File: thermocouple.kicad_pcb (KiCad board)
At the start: 2 copper layers, 39 parts, among them CON1 AVR-ISP-6, IC1 SP3485CN, IC2 ATTINY1634-S, P1 CONN_2, P2 CONN_4, U1 AD8237, U2 TC1047, U3 7805, U4 LM358, X1 CRYSTAL

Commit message: visko daug
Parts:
- added 1PIN_SMD: P***, 1PIN_SMD, F.Cu at (250.4, 150.1)
- added 1PIN_SMD: P***, 1PIN_SMD, F.Cu at (229.5, 150.4)
- added ?: , hole3mm, F.Cu at (215.4, 149.9)
- added C17: 100nF, SM0603_Capa, F.Cu at (265.0, 151.3)
- C1, C12, C5, CON1, JP1, P2, X1: moved to B.Cu
- IC2: value ATTINY1634-S -> ATMEGA88-A; footprint SO20L -> TQFP32
- R9: value 120 -> 10k
- U3: footprint TO220 -> LM78XXV; moved to B.Cu
- moved CON1 270.5 mm to (205.4, 176.0), turned to 270 degrees
- moved C2 93.3 mm to (255.0, 141.9), turned to 180 degrees
- moved L1 90.6 mm to (254.9, 140.1), turned to 180 degrees
- moved C4 90.4 mm to (254.9, 138.2), turned to 0 degrees
- moved D???1 84.4 mm to (251.7, 141.4), turned to 270 degrees
- moved R5 84.1 mm to (251.7, 138.8), turned to 90 degrees
- moved P1 82.4 mm to (240.0, 150.0), turned to 270 degrees
- moved P2 73.3 mm to (261.2, 150.0), turned to 90 degrees
- moved C15 72.4 mm to (257.3, 163.6)
- moved U2 72.2 mm to (235.3, 137.5)
- moved R1 72.0 mm to (241.8, 141.1), turned to 0 degrees
- moved C14 69.6 mm to (241.3, 161.9), turned to 90 degrees
- moved C7 66.0 mm to (243.1, 134.5), turned to 0 degrees
- moved X1 65.8 mm to (239.5, 162.3), turned to 135 degrees
- moved C6 65.5 mm to (254.1, 131.2), turned to 225 degrees
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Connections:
- net N-0000010 renamed /VTHERMO_FILTERED
- net N-0000013 renamed /TERMINATOR
- net N-000002 renamed /FB
- net N-000004 renamed /THERMOCOUPLE+
- C14 pad 1: N-0000018 -> N-0000016
- IC1 pad 1: N-0000026 -> /RX
- IC1 pad 2: N-0000029 -> //RE
- IC1 pad 3: N-0000029 -> //RE
- IC1 pad 4: N-0000031 (its old number) -> /TX
- IC1 pad 7: /B -> VDD
- IC2 pad 1: N-0000031 (its old number) -> N-0000041
- IC2 pad 10: GND -> N-0000037
- IC2 pad 11: VDD -> N-0000036
- IC2 pad 12: N-0000018 -> N-0000028
- IC2 pad 13: N-000007 -> N-0000026
- IC2 pad 14: N-000005 -> N-0000025
- IC2 pad 18: N-0000033 (its old number) -> VAA
- IC2 pad 2: N-0000026 -> N-0000040
- IC2 pad 20: N-0000019 -> /AREF
- IC2 pad 3: N-0000029 -> GND
- IC2 pad 4: N-0000023 (its old number) -> VDD
- IC2 pad 5: /THERMOCOUPLE -> GND
- IC2 pad 6: /AMBIENT_TEMP -> VDD
- IC2 pad 7: N-0000017 (its old number) -> N-0000016
- IC2 pad 8: N-0000021 (its old number) -> N-000007
- IC2 pad 9: /AREF -> N-0000038
- P1 pad 1: N-000003 (its old number) -> /THERMOCOUPLE-
- R1 pad 1: N-000003 (its old number) -> /THERMOCOUPLE-
- R9 pad 1: N-000005 -> VDD
- R9 pad 2: VDD -> N-0000014
- U1 pad 3: N-000003 (its old number) -> /THERMOCOUPLE-
- U4 pad 6: /THERMOCOUPLE -> /VTHERMO_BUFFERED
- U4 pad 7: /THERMOCOUPLE -> /VTHERMO_BUFFERED
- X1 pad 1: N-0000018 -> N-0000016
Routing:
- net /VTHERMO_BUFFERED: track 0.00 -> 64.4 mm
- net /AMBIENT_TEMP: track 2.09 -> 60.4 mm
- net VAA: track 33.8 -> 47.9 mm, vias 0 -> 1
- net N-0000046: track 15.4 -> 2.33 mm
- net N-000003 (its old number): track 12.2 -> 0.00 mm
- net /THERMOCOUPLE+: track 12.2 -> 0.00 mm
- net VCC: track 1.64 -> 11.0 mm
- net GND: track 6.69 -> 1.41 mm
- net N-0000016: track 0.00 -> 5.21 mm
- net VDD: track 2.43 -> 7.53 mm
- net /AREF: track 6.62 -> 1.54 mm
- net /VTHERMO_FILTERED: track 15.6 -> 10.6 mm
- net N-000007: track 0.00 -> 3.65 mm
- net /THERMOCOUPLE: track 0.65 -> 0.00 mm
- added copper zone on B.Cu, net GND
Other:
- board outline added: 54.9 x 54.9 mm

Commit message: blah
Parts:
- removed P1: CONN_2, PIN_ARRAY_2X1
- added ?: , hole3mm, F.Cu at (238.3, 172.6)
- added ?: , hole3mm, F.Cu at (256.4, 148.7)
- added C18: 100nF, SM0603_Capa, F.Cu at (229.4, 137.0)
- added C19: 10uF, SM0805, B.Cu at (237.2, 134.2)
- added C20: 100nF, SM0603_Capa, B.Cu at (232.7, 127.3)
- added C21: 100nF, SM0603_Capa, F.Cu at (273.9, 144.0)
- added C22: 10nF, SM0603_Capa, F.Cu at (269.4, 140.3)
- added C23: 1nF, SM0603_Capa, F.Cu at (269.4, 138.4)
- added D1: DIODE, DO-214AA(SMB), F.Cu at (262.4, 141.2)
- added D2: DIODE, DO-214AC(SMA), F.Cu at (224.9, 183.6)
- added D3: DIODE, DO-214AC(SMA), F.Cu at (223.9, 190.1)
- added R11: 1k, SM0603_Resistor, F.Cu at (243.1, 134.0)
- added R12: 1k 1%, SM0603_Resistor, F.Cu at (234.9, 126.6)
- added R13: 100k 1%, SM0603_Resistor, F.Cu at (232.7, 127.3)
- added R14: 10k, SM0603_Resistor, F.Cu at (230.0, 133.7)
- added R15: 1k, SM0603_Resistor, F.Cu at (252.5, 138.8)
- 1PIN_SMD (x2), C16, C17, C7: moved to B.Cu
- R2: value R -> 1k 0.1%; footprint SM0603 -> SM0805
- R3: value R -> 100k 0.1%; footprint SM0603 -> SM0805
- R4, R6: value 1k -> 1k 0.1%; footprint SM0603 -> SM0805
- R5: value R -> 1k
- U4: value LM358 -> MCP6L01
- moved C16 47.9 mm to (251.1, 156.1), turned to 0 degrees
- moved CON1 42.8 mm to (247.5, 168.8)
- moved C17 39.7 mm to (227.3, 163.8), turned to 270 degrees
- moved R9 37.5 mm to (241.9, 166.4), turned to 270 degrees
- moved IC1 17.0 mm to (255.9, 161.5), turned to 0 degrees
- moved JP1 13.1 mm to (259.7, 160.9), turned to 90 degrees
- moved C3 12.3 mm to (270.0, 135.2)
- moved R8 9.38 mm to (261.6, 161.7), turned to 270 degrees
- moved 1PIN_SMD 8.89 mm to (231.6, 141.7), turned to 90 degrees
- moved 1PIN_SMD 8.72 mm to (248.0, 141.7), turned to 270 degrees
- moved C15 7.10 mm to (256.0, 156.6), turned to 0 degrees
- moved C1 3.84 mm to (257.2, 141.1), turned to 45 degrees
- moved C5 3.02 mm to (251.5, 129.5), turned to 335 degrees
- moved R1 2.96 mm to (244.0, 139.1), turned to 90 degrees
- moved C2 2.60 mm to (257.6, 141.9)
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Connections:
- 1PIN_SMD pad 1: (no net) -> /THERMOCOUPLE-
- 1PIN_SMD pad 1: (no net) -> /THERMOCOUPLE+
- CON1 pad 1: N-0000011 (its old number) -> /MISO
- CON1 pad 2: N-0000035 -> VDD
- CON1 pad 3: N-0000034 -> /SCK
- CON1 pad 4: N-0000033 -> /MOSI
- CON1 pad 5: N-0000032 -> /RESET
- CON1 pad 6: N-0000031 -> GND
- IC1 pad 7: VDD -> /B
- IC1 pad 8: (no net) -> VDD
- IC2 pad 15: N-0000024 -> /MOSI
- IC2 pad 16: N-0000023 -> /MISO
- IC2 pad 17: N-0000021 -> /SCK
- IC2 pad 24: /VTHERMO_BUFFERED -> /VTHERMO_FILTERED
- IC2 pad 29: N-0000014 (its old number) -> /RESET
- P2 pad 2: /B -> /A
- P2 pad 3: /A -> /B
- P2 pad 4: VCC -> N-0000038
- R1 pad 2: GND -> N-0000045
- R2 pad 1: GND -> /FB
- R2 pad 2: /FB -> N-0000045
- R6 pad 2: /AMBIENT_TEMP -> N-0000048
- R9 pad 2: N-0000014 (its old number) -> /RESET
- U1 pad 6: GND -> N-0000030
- U4 pad 1: /AMBIENT_TEMP -> N-0000048
- U4 pad 5: /VTHERMO_FILTERED -> N-0000028
- U4 pad 6: /VTHERMO_BUFFERED -> N-0000045
- U4 pad 7: /VTHERMO_BUFFERED -> N-0000045
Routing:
- net /AREF: track 1.54 -> 94.1 mm, vias 0 -> 5
- net VDD: track 7.53 -> 74.7 mm, vias 0 -> 2
- net /VTHERMO_BUFFERED: track 64.4 -> 0.00 mm
- net VAA: track 47.9 -> 105.5 mm, vias 1 -> 6
- net /VTHERMO_FILTERED: track 10.6 -> 61.0 mm
- net GND: track 1.41 -> 49.7 mm, vias 0 -> 24
- net /TX: track 0.00 -> 33.8 mm
- net /RX: track 0.00 -> 32.2 mm
- net //RE: track 0.00 -> 30.7 mm
- net /B: track 0.00 -> 28.2 mm
- net /SCK: track 0.00 -> 26.8 mm, vias 0 -> 1
- net /MISO: track 0.00 -> 24.0 mm, vias 0 -> 1
- net /MOSI: track 0.00 -> 22.9 mm, vias 0 -> 2
- net N-0000045: track 0.00 -> 22.1 mm, vias 0 -> 2
- net /RESET: track 0.00 -> 22.1 mm, vias 0 -> 2
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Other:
- board size 54.9 x 54.9 mm -> 55 x 55 mm
- net class Default: via_dia 0.889 -> 0.762; via_drill 0.635 -> 0.381
- net class power: via_dia 0.889 -> 0.762; via_drill 0.635 -> 0.381
- rule via_min_drill: 0.508 -> 0.381
- rule via_min_size: 0.889 -> 0.762

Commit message: suddenly everything went better than expected
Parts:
- added D4: LED, SM0805, B.Cu at (227.6, 159.2)
- added D5: LED, SM0805, B.Cu at (227.6, 161.4)
- added R10: 1k, SM0603_Resistor, B.Cu at (224.3, 159.2)
- added R16: 1k, SM0603_Resistor, B.Cu at (224.3, 161.4)
- C1, C5: footprint c_tant_E -> C1V8
- C3: moved to B.Cu
- CON1: moved to F.Cu
- R1, R5, R7, R8, R9: footprint SM0603 -> SM0603_Resistor
- moved C5 25.6 mm to (253.7, 155.0), turned to 90 degrees
- moved CON1 24.8 mm to (227.4, 154.2)
- moved C3 11.8 mm to (258.4, 137.6), turned to 225 degrees
- moved C23 9.63 mm to (274.0, 146.9)
- moved C6 6.74 mm to (249.0, 135.6), turned to 180 degrees
- moved L2 6.28 mm to (248.9, 133.6), turned to 180 degrees
- moved R8 5.84 mm to (260.6, 156.0), turned to 180 degrees
- moved C8 4.78 mm to (247.2, 131.4), turned to 180 degrees
- moved C1 4.47 mm to (255.1, 145.0), turned to 180 degrees
- moved C9 3.05 mm to (247.2, 129.5), turned to 180 degrees
- moved IC1 2.79 mm to (253.4, 160.3), turned to 270 degrees
- moved C10 2.39 mm to (247.2, 127.7), turned to 180 degrees
- moved JP1 2.26 mm to (261.3, 159.3), turned to 270 degrees
- moved C17 2.19 mm to (225.1, 163.9)
- moved C22 1.47 mm to (269.6, 138.9)
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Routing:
- net GND: track 49.7 -> 123.1 mm, vias 24 -> 66
- net VDD: track 74.7 -> 97.5 mm, vias 2 -> 5
- net /SCK: track 26.8 -> 9.85 mm, vias 1 -> 0
- net /MOSI: track 22.9 -> 7.30 mm, vias 2 -> 0
- net /B: track 28.2 -> 14.4 mm
- net /MISO: track 24.0 -> 11.2 mm, vias 1 -> 0
- net /A: track 17.4 -> 29.8 mm
- net /TX: track 33.8 -> 21.8 mm
- net //RE: track 30.7 -> 20.8 mm
- net /RX: track 32.2 -> 24.2 mm
- net /AREF: track 94.1 -> 87.1 mm
- net N-0000027: track 0.00 -> 6.24 mm, vias 0 -> 1
- net N-0000026: track 0.00 -> 5.84 mm, vias 0 -> 1
- net VCC: track 10.5 -> 16.0 mm
- net /RESET: track 22.1 -> 27.6 mm
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
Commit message: almost there
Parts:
- removed D2, D3: DIODE, DO-214AC(SMA)
- removed P2: CONN_4, PIN_ARRAY_4x1
- added C101: 100nF, SM0603_Capa, F.Cu at (222.8, 132.2)
- added C102: 100nF, SM0603_Capa, B.Cu at (236.9, 165.3)
- added C103: 100nF, SM0603_Capa, B.Cu at (234.0, 163.2)
- added C104: 100nF, SM0603_Capa, F.Cu at (225.1, 145.9)
- added C105: 100nF, SM0603_Capa, B.Cu at (227.7, 165.0)
- added C106: 100nF, SM0603_Capa, B.Cu at (246.0, 165.4)
- added C107: 10uF, SM0805, F.Cu at (220.9, 165.3)
- added P10: 12AC, conn35, B.Cu at (262.3, 146.1)
- added P10: 12AC, conn35, B.Cu at (262.3, 153.7)
- added R17: 1k, SM0603_Resistor, F.Cu at (233.8, 140.9)
- added R18: 1k, SM0603_Resistor, F.Cu at (244.1, 139.7)
- C21: moved to B.Cu
- moved C21 43.9 mm to (234.2, 125.5)
- moved C23 23.4 mm to (253.1, 136.4)
- moved C22 13.9 mm to (255.9, 136.4), turned to 180 degrees
- moved R8 3.29 mm to (259.0, 158.9), turned to 90 degrees
- moved C16 3.27 mm to (247.9, 155.3), turned to 90 degrees
- moved D1 2.21 mm to (261.6, 139.7)
- moved R1 1.78 mm to (244.0, 137.3)
- moved C19 1.73 mm to (238.4, 132.9)
- moved C1 0.99 mm to (254.6, 144.1)
- moved C5 0.76 mm to (253.0, 154.9)
- moved JP1 0.74 mm to (261.1, 160.0)
- moved C12 0.27 mm to (232.1, 130.7)
- moved C2 0.23 mm to (257.4, 142.0)
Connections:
- C21 pad 1: N-0000025 -> N-000007
- C22 pad 1: N-0000024 -> N-0000049
- C23 pad 1: N-0000023 -> N-0000049
- C4 pad 1: N-0000052 -> N-0000049
- D1 pad 1: N-0000035 -> /VIN
- L1 pad 2: N-0000052 -> N-0000049
- R12 pad 2: N-0000036 -> N-000007
- R13 pad 1: N-0000036 -> N-000007
- R15 pad 2: N-0000052 -> N-0000049
- R5 pad 2: N-0000052 -> N-0000049
- U1 pad 2: /THERMOCOUPLE+ -> N-0000030
- U1 pad 3: /THERMOCOUPLE- -> N-0000029
- U4 pad 5: N-0000036 -> N-000007
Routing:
- net GND: track 123.1 -> 161.0 mm, vias 66 -> 84
- net N-0000049: track 0.00 -> 9.76 mm
- net /A: track 29.8 -> 21.3 mm
- net /THERMOCOUPLE+: track 9.55 -> 1.88 mm
- net N-000007: track 0.00 -> 7.40 mm, vias 0 -> 1
- net N-0000030: track 0.00 -> 6.47 mm
- net N-0000052: track 6.23 -> 0.00 mm
- net N-0000029: track 0.00 -> 4.21 mm
- net N-0000036: track 4.11 -> 0.00 mm
- net /AREF: track 87.1 -> 91.0 mm, vias 5 -> 6
- net VAA: track 107.4 -> 111.1 mm
- net /THERMOCOUPLE-: track 9.48 -> 6.04 mm
- net /VIN: track 0.00 -> 2.86 mm
- net /B: track 14.4 -> 11.8 mm
- net N-0000035: track 2.33 -> 0.00 mm
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
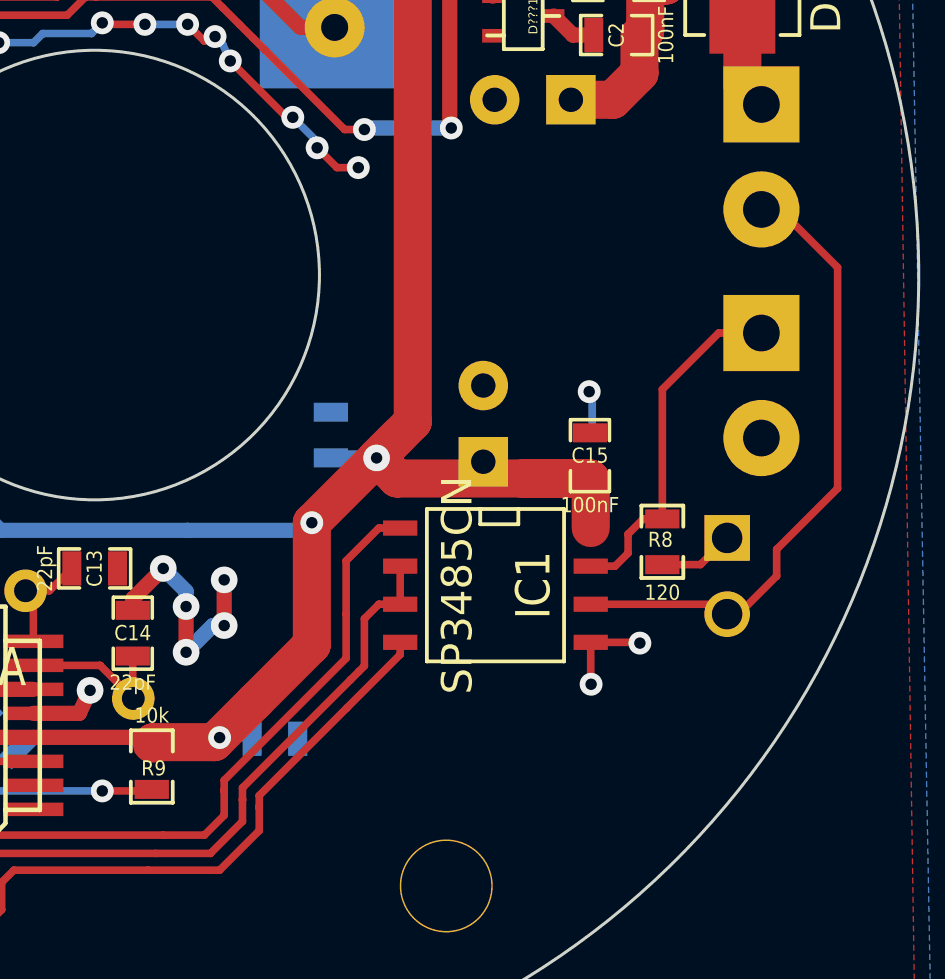
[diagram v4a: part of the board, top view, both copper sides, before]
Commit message: RS485 protection added
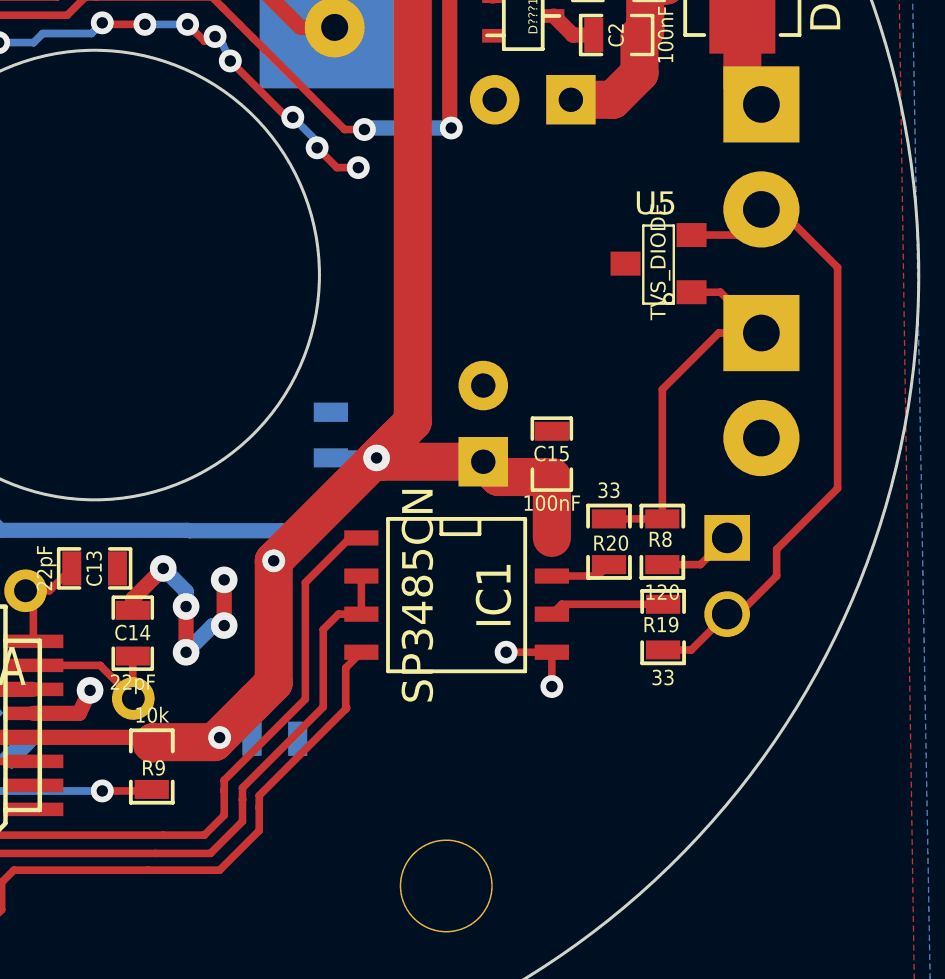
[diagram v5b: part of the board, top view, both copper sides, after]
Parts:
- added R19: 33, SM0603_Resistor, F.Cu at (259.0, 161.7)
- added R20: 33, SM0603_Resistor, F.Cu at (257.2, 158.9)
- added U5: TVS_DIODE, SOT23, F.Cu at (258.8, 149.6)
- moved IC1 1.34 mm to (252.1, 160.7)
- moved C15 1.27 mm to (255.3, 156.0)
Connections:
- IC1 pad 6: /A -> N-0000029
- IC1 pad 7: /B -> N-0000028
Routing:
- net VDD: track 97.7 -> 92.4 mm
- net N-0000029: track 0.00 -> 3.85 mm
- net N-0000028: track 0.00 -> 2.06 mm
- net (no net): track 1.44 -> 0.00 mm, vias 1 -> 0
- net /B: track 11.8 -> 13.1 mm
- net //RE: track 20.8 -> 19.9 mm
- net /TX: track 21.8 -> 21.0 mm
- net /RX: track 24.2 -> 23.6 mm
- net /A: track 21.3 -> 22.0 mm

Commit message: more stuff
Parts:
- added C110: 10uF, SM0805, F.Cu at (238.9, 171.8)
- added P3: CONN_4, PIN_ARRAY_4x1, B.Cu at (232.4, 172.7)
- renumbered CON1 to AVR-ISP
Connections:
- IC2 pad 27: N-0000012 (its old number) -> /SDA
- IC2 pad 28: N-0000010 -> /SCL
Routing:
- net VDD: track 92.4 -> 110.0 mm, vias 5 -> 6
- net GND: track 160.6 -> 166.3 mm, vias 84 -> 87
- net /SCL: track 0.00 -> 3.29 mm
- net /SDA: track 0.00 -> 3.28 mm
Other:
- board text added: "5V SCL SDA GND"
- board text added: "MODBUS-THERMOCOUPLE V1.0 mic@wemakethings.net, 2013 OSHL 1.1"
- board text added: "RS485 term"
- board text added: "VCC A B GND"

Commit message: still fiddling around
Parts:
- moved D???1 130.8 mm to (146.7, 67.1)
- moved R15 130.6 mm to (145.2, 64.4)
- moved 1PIN_SMD 130.5 mm to (140.8, 67.3)
- moved ? 130.5 mm to (108.2, 75.4)
- moved ? 130.5 mm to (131.1, 98.2)
- moved ? 130.5 mm to (149.2, 74.3)
- moved AVR-ISP 130.5 mm to (120.2, 79.8)
- moved C1 130.5 mm to (147.4, 69.7)
- moved C10 130.5 mm to (140.0, 53.2)
- moved C101 130.5 mm to (115.6, 57.8)
- moved C103 130.5 mm to (126.8, 88.7)
- moved C106 130.5 mm to (138.8, 91.0)
- moved C11 130.5 mm to (135.5, 55.4)
- moved C12 130.5 mm to (124.9, 56.3)
- moved C14 130.5 mm to (134.1, 87.5)
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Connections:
- D???1 pad 1: /AREF -> N-0000052
- R5 pad 1: /AREF -> N-0000052
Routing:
- net GND: track 166.3 -> 196.8 mm, vias 87 -> 102
- net /AREF: track 91.0 -> 87.7 mm
- net N-0000052: track 0.00 -> 2.04 mm
- net VDD: track 110.0 -> 109.1 mm
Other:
- board text added: "GND SDA SCL 5V"
- board text removed: "5V SCL SDA GND"

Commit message: testing and calibration was going on
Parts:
- ? (x2): renamed from P10; value 12AC -> (none)
- D1: value DIODE -> (none)
- D4, D5: value LED -> (none)
- T+, T-: renamed from 1PIN_SMD; value P*** -> (none)
- X1: value CRYSTAL -> (none)
- moved C12 0.60 mm to (125.5, 56.5)
- moved C4 0.06 mm to (150.4, 63.8)
- renumbered JP1 to ?, P3 to ?, D???1 to REF
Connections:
- R5 pad 1: N-0000052 -> /AREF
- REF pad 1: N-0000052 -> /AREF
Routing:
- net /AREF: track 87.7 -> 91.9 mm
- net N-0000052: track 2.04 -> 0.00 mm
- net VAA: track 111.1 -> 110.1 mm
- net /A: track 22.0 -> 22.6 mm
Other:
- net class storesni added: clearance 0.254, trace_width 0.508, via_dia 0.762, via_drill 0.381
